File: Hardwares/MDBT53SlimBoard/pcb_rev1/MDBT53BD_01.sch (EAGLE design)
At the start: 37 parts, among them CN1 IF_6PIN, CN2 USB4105-GF-A, CN3 51296-0894, Q1 BSS84AKQBZ, U1 RV-3028-C7, U2 XC6206P302MR-G

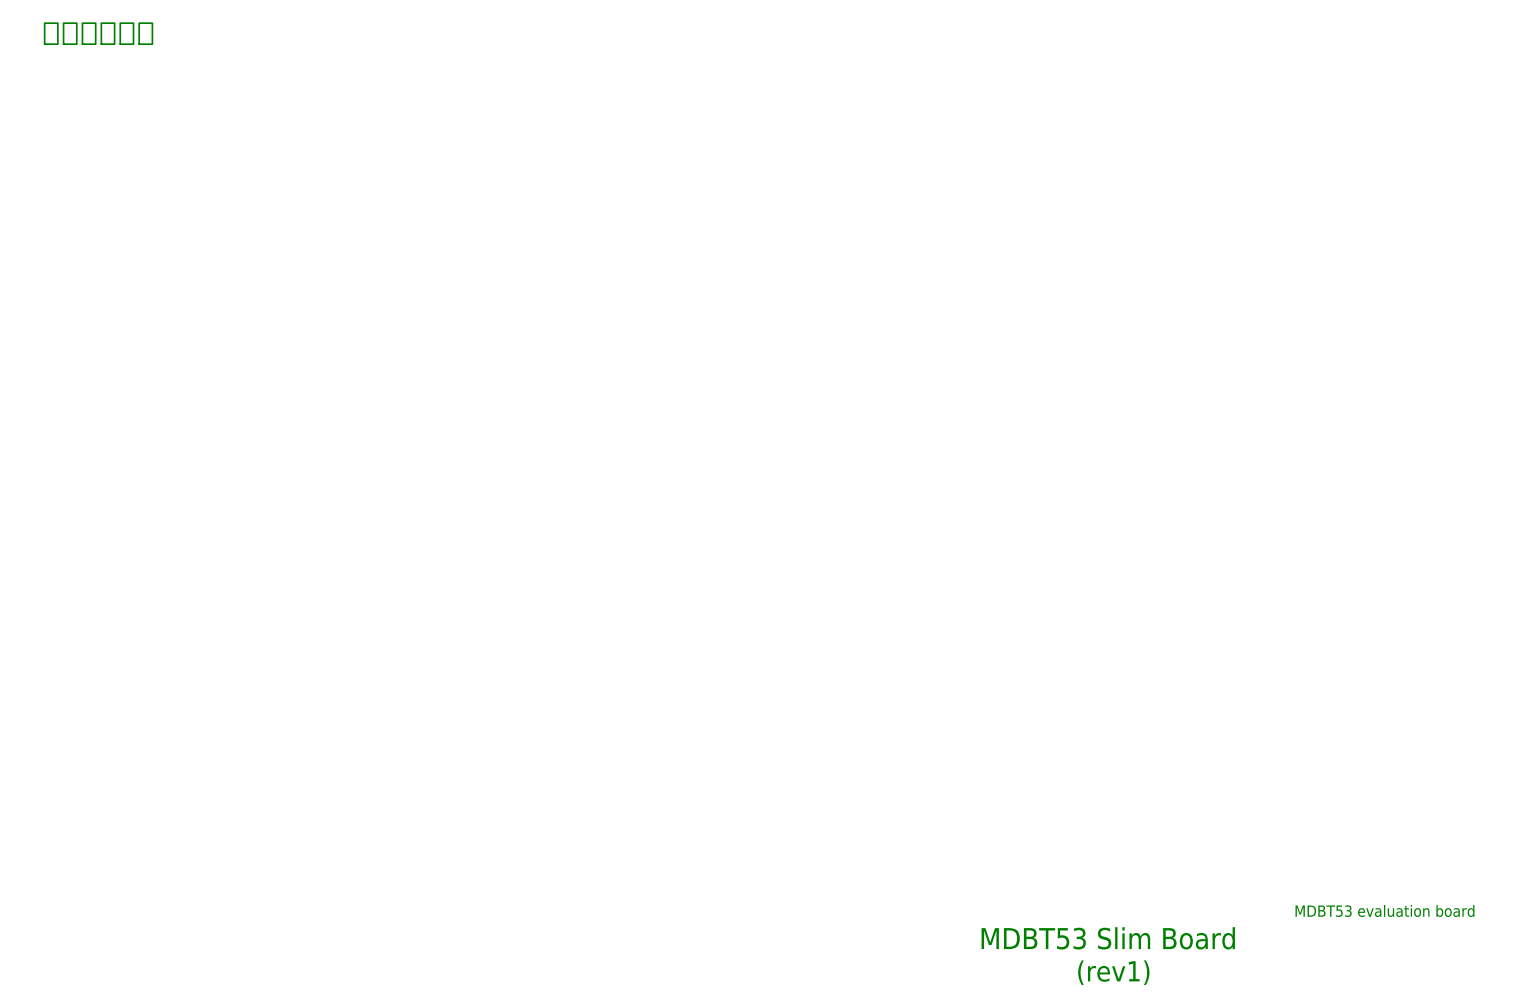
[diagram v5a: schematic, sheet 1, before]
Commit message: 回路図の作成
・モジュール部の周辺回路／部品を追加
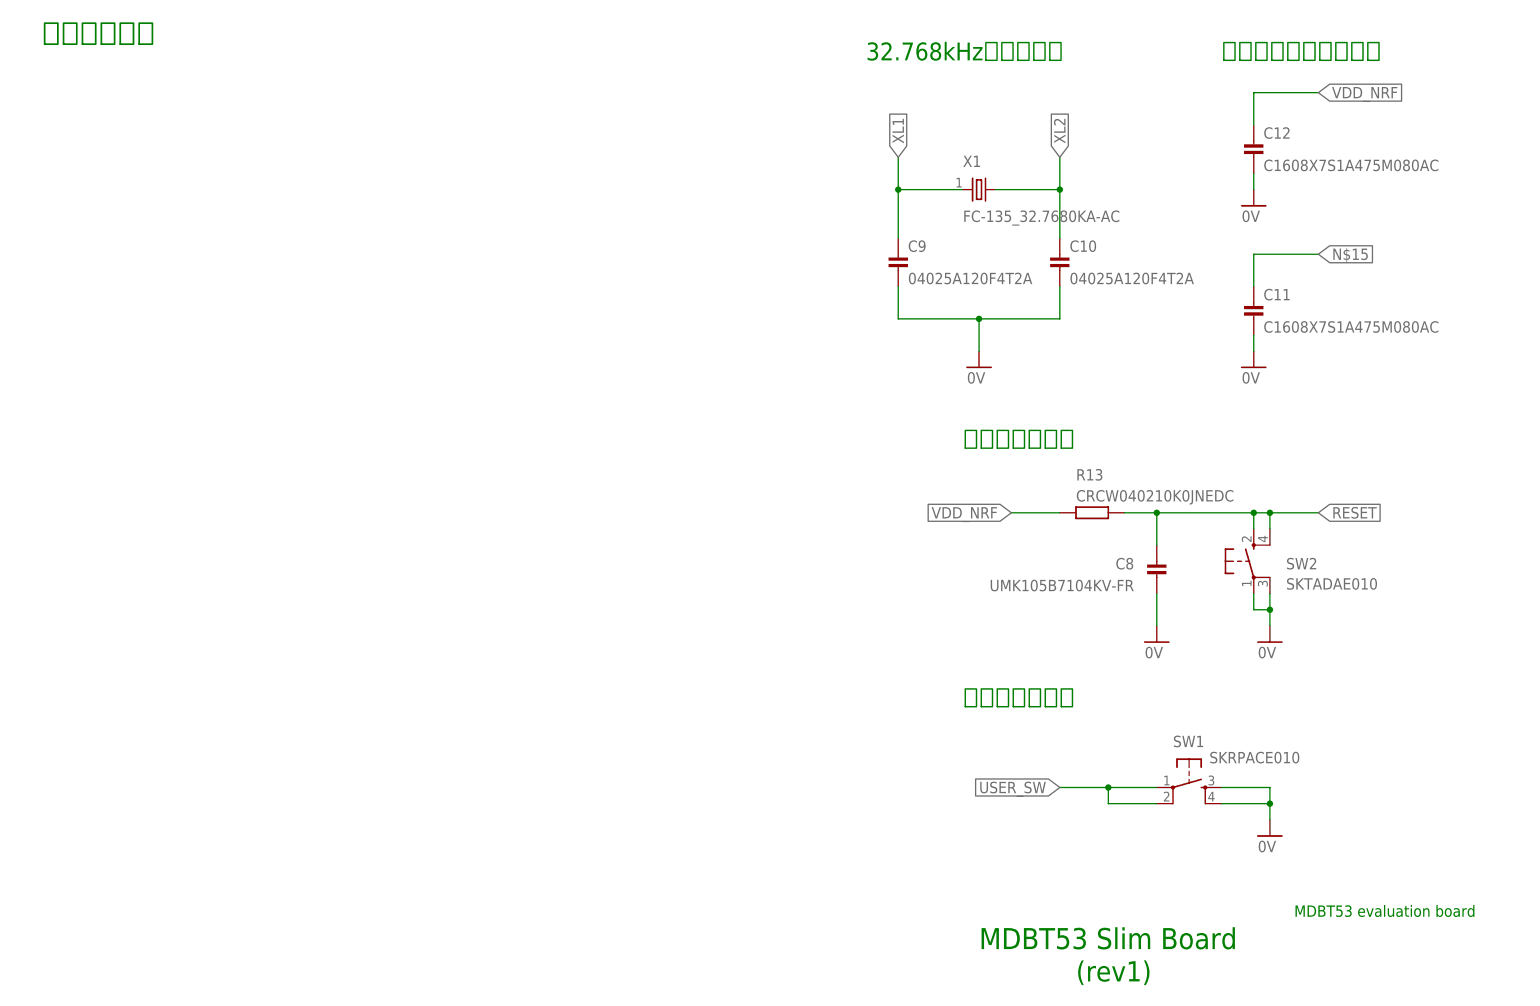
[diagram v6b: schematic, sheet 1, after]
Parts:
- added C10, C9: 04025A120F4T2A, Parts:CAP_0402K
- added C11, C12: C1608X7S1A475M080AC, Parts:CAP_0603N
- added C8: UMK105B7104KV-FR, Parts:CAP_0402K
- added R13: CRCW040210K0JNEDC, Parts:RESISTOR_0402N
- added SW1: SKRPACE010, Parts:SKRPACE010
- added SW2: SKTADAE010, Parts:SKTADAE010
- added X1: FC-135_32.7680KA-AC, Parts:FC-135_32.7680KA-AC
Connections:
- new net N$15: C11.1
- new net USER_SW: SW1.P, SW1.P1
- new net XL1: C9.1, X1.1
- new net XL2: C10.1, X1.2
- net 0V: now also C10.2, C11.2, C12.2, C8.2, C9.2, SW1.S, SW1.S1, SW2.P, SW2.P1
- net RESET: now also C8.1, R13.2, SW2.S, SW2.S1
- net VDD_NRF: now also C12.1, R13.1
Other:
- note added: "32.768kHzクリスタル"
- note added: "バイパスコンデンサー"
- note added: "ユーザーボタン"
- note added: "リセットボタン"
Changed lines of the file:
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@@
 <part name="R12" library="Parts" deviceset="RESISTOR" device="_0402N"/>
 <part name="Q1" library="Parts" deviceset="BSS84AKQB" device="Z"/>
+<part name="SW1" library="Parts" deviceset="SKRPACE010" device=""/>
+<part name="SW2" library="Parts" deviceset="SKTADAE010" device=""/>
+<part name="GND14" library="Supply" deviceset="0V" device=""/>
+<part name="GND15" library="Supply" deviceset="0V" device=""/>
+<part name="GND16" library="Supply" deviceset="0V" device=""/>
+<part name="GND17" library="Supply" deviceset="0V" device=""/>
+<part name="GND18" library="Supply" deviceset="0V" device=""/>
+<part name="GND19" library="Supply" deviceset="0V" device=""/>
+<part name="C8" library="Parts" deviceset="CAP" device="_0402K" value="UMK105B7104KV-FR"/>
+<part name="C9" library="Parts" deviceset="CAP" device="_0402K" value="04025A120F4T2A"/>
+<part name="C10" library="Parts" deviceset="CAP" device="_0402K" value="04025A120F4T2A"/>
+<part name="C11" library="Parts" deviceset="CAP" device="_0603N" value="C1608X7S1A475M080AC"/>
+<part name="C12" library="Parts" deviceset="CAP" device="_0603N" value="C1608X7S1A475M080AC"/>
+<part name="X1" library="Parts" deviceset="FC-135_32.7680KA" device="-AC"/>
+<part name="R13" library="Parts" deviceset="RESISTOR" device="_0402N" value="CRCW040210K0JNEDC"/>
 </parts>
 <sheets>
@@
 <text x="217.17" y="20.32" size="1.778" layer="91">MDBT53 evaluation board</text>
 <text x="20.32" y="157.48" size="3.302" layer="91">モジュール部</text>
+<text x="149.86" y="154.94" size="2.794" layer="91">32.768kHzクリスタル</text>
+<text x="205.74" y="154.94" size="2.794" layer="91">バイパスコンデンサー</text>
+<text x="165.1" y="93.98" size="2.794" layer="91">リセットボタン</text>
+<text x="165.1" y="53.34" size="2.794" layer="91">ユーザーボタン</text>
 </plain>
 <instances>
 <instance part="FRAME1" gate="G$1" x="0" y="0"/>
+<instance part="SW1" gate="G$1" x="200.66" y="40.64" rot="R270"/>
+<instance part="SW2" gate="G$1" x="210.82" y="76.2" smashed="yes">
+<attribute name="NAME" x="215.9" y="74.93" size="1.778" layer="95"/>
+<attribute name="VALUE" x="215.9" y="71.755" size="1.778" layer="96"/>
+</instance>
+<instance part="GND14" gate="1" x="195.58" y="63.5"/>
+<instance part="GND15" gate="1" x="213.36" y="63.5"/>
+<instance part="GND16" gate="1" x="213.36" y="33.02"/>
+<instance part="GND17" gate="1" x="210.82" y="106.68"/>
+<instance part="GND18" gate="1" x="210.82" y="132.08"/>
+<instance part="GND19" gate="1" x="167.64" y="106.68"/>
+<instance part="C8" gate="G$1" x="195.58" y="78.74" smashed="yes">
+<attribute name="NAME" x="192.024" y="74.93" size="1.778" layer="95" align="bottom-right"/>
+<attribute name="VALUE" x="192.024" y="71.501" size="1.778" layer="96" align="bottom-right"/>
+</instance>
+<instance part="C9" gate="G$1" x="154.94" y="127"/>
+<instance part="C10" gate="G$1" x="180.34" y="127"/>
+<instance part="C11" gate="G$1" x="210.82" y="119.38"/>
+<instance part="C12" gate="G$1" x="210.82" y="144.78"/>
+<instance part="X1" gate="G$1" x="167.64" y="134.62" smashed="yes">
+<attribute name="NAME" x="165.1" y="138.176" size="1.778" layer="95"/>
+<attribute name="VALUE" x="165.1" y="129.54" size="1.778" layer="96"/>
+</instance>
+<instance part="R13" gate="G$1" x="180.34" y="83.82" smashed="yes">
+<attribute name="NAME" x="182.88" y="88.9" size="1.778" layer="95"/>
+<attribute name="VALUE" x="182.88" y="85.598" size="1.778" layer="96"/>
+</instance>
 </instances>
 <busses>
 </busses>
 <nets>
+<net name="0V" class="0">
+<segment>
+<pinref part="SW1" gate="G$1" pin="S1"/>
+<pinref part="GND16" gate="1" pin="0V"/>
+<wire x1="205.74" y1="38.1" x2="213.36" y2="38.1" width="0.1524" layer="91"/>
+<wire x1="213.36" y1="38.1" x2="213.36" y2="35.56" width="0.1524" layer="91"/>
+<pinref part="SW1" gate="G$1" pin="S"/>
+<wire x1="205.74" y1="40.64" x2="213.36" y2="40.64" width="0.1524" layer="91"/>
+<wire x1="213.36" y1="40.64" x2="213.36" y2="38.1" width="0.1524" layer="91"/>
+<junction x="213.36" y="38.1"/>
+</segment>
+<segment>
+<pinref part="GND18" gate="1" pin="0V"/>
+<pinref part="C12" gate="G$1" pin="2"/>
+<wire x1="210.82" y1="134.62" x2="210.82" y2="137.16" width="0.1524" layer="91"/>
+</segment>
+<segment>
+<pinref part="C11" gate="G$1" pin="2"/>
+<pinref part="GND17" gate="1" pin="0V"/>
+<wire x1="210.82" y1="111.76" x2="210.82" y2="109.22" width="0.1524" layer="91"/>
+</segment>
+<segment>
+<pinref part="C9" gate="G$1" pin="2"/>
+<wire x1="154.94" y1="119.38" x2="154.94" y2="114.3" width="0.1524" layer="91"/>
+<pinref part="GND19" gate="1" pin="0V"/>
+<wire x1="154.94" y1="114.3" x2="167.64" y2="114.3" width="0.1524" layer="91"/>
+<wire x1="167.64" y1="114.3" x2="167.64" y2="109.22" width="0.1524" layer="91"/>
+<pinref part="C10" gate="G$1" pin="2"/>
+<wire x1="167.64" y1="114.3" x2="180.34" y2="114.3" width="0.1524" layer="91"/>
+<wire x1="180.34" y1="114.3" x2="180.34" y2="119.38" width="0.1524" layer="91"/>
+<junction x="167.64" y="114.3"/>
+</segment>
+<segment>
+<pinref part="C8" gate="G$1" pin="2"/>
+<pinref part="GND14" gate="1" pin="0V"/>
+<wire x1="195.58" y1="71.12" x2="195.58" y2="66.04" width="0.1524" layer="91"/>
+</segment>
+<segment>
+<pinref part="SW2" gate="G$1" pin="P"/>
+<wire x1="210.82" y1="71.12" x2="210.82" y2="68.58" width="0.1524" layer="91"/>
+<wire x1="210.82" y1="68.58" x2="213.36" y2="68.58" width="0.1524" layer="91"/>
+<pinref part="GND15" gate="1" pin="0V"/>
+<wire x1="213.36" y1="68.58" x2="213.36" y2="66.04" width="0.1524" layer="91"/>
+<pinref part="SW2" gate="G$1" pin="P1"/>
+<wire x1="213.36" y1="68.58" x2="213.36" y2="71.12" width="0.1524" layer="91"/>
+<junction x="213.36" y="68.58"/>
+</segment>
+</net>
+<net name="USER_SW" class="0">
+<segment>
+<pinref part="SW1" gate="G$1" pin="P1"/>
+<wire x1="195.58" y1="38.1" x2="187.96" y2="38.1" width="0.1524" layer="91"/>
+<wire x1="187.96" y1="38.1" x2="187.96" y2="40.64" width="0.1524" layer="91"/>
+<pinref part="SW1" gate="G$1" pin="P"/>
+<wire x1="195.58" y1="40.64" x2="187.96" y2="40.64" width="0.1524" layer="91"/>
+<label x="180.34" y="40.64" size="1.778" layer="95" rot="R180" xref="yes"/>
+<junction x="187.96" y="40.64"/>
+<wire x1="187.96" y1="40.64" x2="180.34" y2="40.64" width="0.1524" layer="91"/>
+</segment>
+</net>
+<net name="N$15" class="0">
+<segment>
+<pinref part="C11" gate="G$1" pin="1"/>
+<wire x1="210.82" y1="119.38" x2="210.82" y2="124.46" width="0.1524" layer="91"/>
+<wire x1="210.82" y1="124.46" x2="220.98" y2="124.46" width="0.1524" layer="91"/>
+<label x="220.98" y="124.46" size="1.778" layer="95" xref="yes"/>
+</segment>
+</net>
+<net name="XL1" class="0">
+<segment>
+<pinref part="C9" gate="G$1" pin="1"/>
+<wire x1="154.94" y1="127" x2="154.94" y2="134.62" width="0.1524" layer="91"/>
+<pinref part="X1" gate="G$1" pin="1"/>
+<wire x1="154.94" y1="134.62" x2="165.1" y2="134.62" width="0.1524" layer="91"/>
+<wire x1="154.94" y1="134.62" x2="154.94" y2="139.7" width="0.1524" layer="91"/>
+<junction x="154.94" y="134.62"/>
+<label x="154.94" y="139.7" size="1.778" layer="95" rot="R90" xref="yes"/>
+</segment>
+</net>
+<net name="XL2" class="0">
+<segment>
+<pinref part="X1" gate="G$1" pin="2"/>
+<pinref part="C10" gate="G$1" pin="1"/>
+<wire x1="170.18" y1="134.62" x2="180.34" y2="134.62" width="0.1524" layer="91"/>
+<wire x1="180.34" y1="134.62" x2="180.34" y2="127" width="0.1524" layer="91"/>
+<wire x1="180.34" y1="134.62" x2="180.34" y2="139.7" width="0.1524" layer="91"/>
+<junction x="180.34" y="134.62"/>
+<label x="180.34" y="139.7" size="1.778" layer="95" rot="R90" xref="yes"/>
+</segment>
+</net>
+<net name="RESET" class="0">
+<segment>
+<pinref part="SW2" gate="G$1" pin="S"/>
+<wire x1="210.82" y1="81.28" x2="210.82" y2="83.82" width="0.1524" layer="91"/>
+<pinref part="C8" gate="G$1" pin="1"/>
+<wire x1="195.58" y1="78.74" x2="195.58" y2="83.82" width="0.1524" layer="91"/>
+<wire x1="195.58" y1="83.82" x2="210.82" y2="83.82" width="0.1524" layer="91"/>
+<junction x="210.82" y="83.82"/>
+<wire x1="210.82" y1="83.82" x2="213.36" y2="83.82" width="0.1524" layer="91"/>
+<pinref part="SW2" gate="G$1" pin="S1"/>
+<wire x1="213.36" y1="83.82" x2="220.98" y2="83.82" width="0.1524" layer="91"/>
+<wire x1="213.36" y1="81.28" x2="213.36" y2="83.82" width="0.1524" layer="91"/>
+<junction x="213.36" y="83.82"/>
+<label x="220.98" y="83.82" size="1.778" layer="95" xref="yes"/>
+<pinref part="R13" gate="G$1" pin="2"/>
+<wire x1="190.5" y1="83.82" x2="195.58" y2="83.82" width="0.1524" layer="91"/>
+<junction x="195.58" y="83.82"/>
+</segment>
+</net>
+<net name="VDD_NRF" class="0">
+<segment>
+<pinref part="R13" gate="G$1" pin="1"/>
+<wire x1="180.34" y1="83.82" x2="172.72" y2="83.82" width="0.1524" layer="91"/>
+<label x="172.72" y="83.82" size="1.778" layer="95" rot="R180" xref="yes"/>
+</segment>
+<segment>
+<pinref part="C12" gate="G$1" pin="1"/>
+<wire x1="210.82" y1="144.78" x2="210.82" y2="149.86" width="0.1524" layer="91"/>
+<wire x1="210.82" y1="149.86" x2="220.98" y2="149.86" width="0.1524" layer="91"/>
+<label x="220.98" y="149.86" size="1.778" layer="95" xref="yes"/>
+</segment>
+</net>
 </nets>
 </sheet>

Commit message: 回路図の作成
・部品番号を振り直し
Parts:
- C1: value 0.1uF -> 04025A120F4T2A; device Parts:CAP_0402N -> Parts:CAP_0402K
- C10: value 04025A120F4T2A -> TMR107B7105KA-T; device Parts:CAP_0402K -> Parts:CAP_0603N
- C11: value C1608X7S1A475M080AC -> TMR107B7105KA-T
- C12: value C1608X7S1A475M080AC -> UMK105B7104KV-FR; device Parts:CAP_0603N -> Parts:CAP_0402N
- C2: value TMR107B7105KA-T -> 04025A120F4T2A; device Parts:CAP_0603N -> Parts:CAP_0402K
- C3: value TMR107B7105KA-T -> C1608X7S1A475M080AC
- C4: value C0603C106M8PACTU -> C1608X7S1A475M080AC
- C5: value C0402C103K5RAC7411 -> UMK105B7104KV-FR; device Parts:CAP_0402N -> Parts:CAP_0402K
- C6: value UMK105B7104KV-FR -> C0402C103K5RAC7411
- C8: device Parts:CAP_0402K -> Parts:CAP_0402N
- C9: value 04025A120F4T2A -> C0603C106M8PACTU; device Parts:CAP_0402K -> Parts:CAP_0603N
- CN1: value IF_6PIN -> USB4105-GF-A; device Connectors:IF_6PIN -> Connectors:USB4105-GF-A
- CN2: value USB4105-GF-A -> IF_6PIN; device Connectors:USB4105-GF-A -> Connectors:IF_6PIN
- D5: value PMEG2005AEA,115 -> PRTR5V0U2X; device Parts:PMEG2005AEA,115 -> Parts:PRTR5V0U2X
- D7: value PRTR5V0U2X -> PMEG2005AEA,115; device Parts:PRTR5V0U2X -> Parts:PMEG2005AEA,115
- R1: value 10k -> CRCW040210K0JNEDC
- R10, R9: value CRCW04025K10FKED -> CRCW040210K0JNEDC
- R11: value (none) -> CRCW040210K0JNEDC
- R12: value (none) -> CRCW040220K0FKEDC
- R13: value CRCW040210K0JNEDC -> CRCW04025K10FKEDC
- R2, R3: value 10k -> CRCW04025K10FKED
- R4: value 10k -> CRCW04021K20FKEDC
- R5: value 1.2k -> CRCW04021K20FKEDC
- R6: value 1.2k -> CRCW04021K50FKEDC
- R7: value 1.5k -> CRCW0402390RFKEDC
- R8: value 390 -> CRCW040210K0JNEDC
- renumbered U1 to U3
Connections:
- net 0V: now also CN2.1, D5.GND, R10.1, R11.1, R2.2, R3.2; no longer CN1.1, D7.GND, R10.2, R3.1, R4.1, R9.2
- net D_N: now also CN1.D_N1, CN1.D_N2, D5.I/O_1; no longer CN2.D_N1, CN2.D_N2, D7.I/O_1
- net D_P: now also CN1.D_P1, CN1.D_P2, D5.I/O_2; no longer CN2.D_P1, CN2.D_P2, D7.I/O_2
- net LED1: now also R4.1; no longer R5.1
- net LED2: now also R5.1; no longer R6.1
- net LED3: now also R6.1; no longer R7.1
- net LED4: now also R7.1; no longer R8.1
- net LED_CTRL: now also R13.1; no longer R11.1
- net N$1: now also R4.2; no longer R5.2
- net N$10: now also CN1.CC1, R2.1; no longer CN2.CC1, R9.1
- net N$11: now also CN1.FG1, CN1.FG2, CN1.FG3, CN1.FG4; no longer CN2.FG1, CN2.FG2, CN2.FG3, CN2.FG4
- net N$12: now also CN1.GND1, CN1.GND2; no longer CN2.GND1, CN2.GND2
- net N$14: now also R13.2; no longer R11.2
- net N$15: now also C4.1; no longer C11.1
- net N$17: now also C6.1, C8.1, C9.1, CN1.VBUS1, CN1.VBUS2, D5.VCC; no longer C4.1, C5.1, C7.1, CN2.VBUS1, CN2.VBUS2, D7.VCC
- net N$2: now also R10.2; no longer R3.2
- net N$3: now also R11.2; no longer R4.2
- net N$4: now also R5.2; no longer R6.2
- net N$5: now also R6.2; no longer R7.2
- net N$6: now also R7.2; no longer R8.2
- net N$7: now also CN1.CC2, R3.1; no longer CN2.CC2, R10.1
- net N$8: now also C11.1, D6.A; no longer C3.1, D5.A
- net N$9: now also D7.A; no longer D6.A
- net RESET: now also C5.1, CN2.5, R1.2; no longer C8.1, CN1.5, R13.2
- net SWDCLK: now also CN2.4; no longer CN1.4
- net SWDIO: now also CN2.3; no longer CN1.3
- net TWI_SCL: now also R9.1; no longer R2.1
- net TWI_SDA: now also R8.1; no longer R1.1
- net TXD: now also CN2.6; no longer CN1.6
- net VBUS_LDO: now also C10.1; no longer C2.1
- net VBUS_NRF: now also C7.1; no longer C6.1
- net VDD_NRF: now also C3.1, CN2.2, D7.C, R1.1, R8.2, R9.2; no longer C1.1, CN1.2, D5.C, R1.2, R13.1, R2.2
- net XL1: now also C1.1; no longer C9.1
- net XL2: now also C2.1; no longer C10.1
